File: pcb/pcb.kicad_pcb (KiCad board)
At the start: 2 copper layers, 173.5 x 140.5 mm, 75 parts, among them J1 RJ45, J2 RJ45, SW1 Keyswitch, SW10 Keyswitch, SW11 Keyswitch, SW12 Keyswitch, SW13 Keyswitch, SW14 Keyswitch, SW15 Keyswitch, SW16 Keyswitch, SW17 Keyswitch, SW18 Keyswitch, SW19 Keyswitch, SW2 Keyswitch, SW20 Keyswitch, SW21 Keyswitch, SW22 Keyswitch, SW23 Keyswitch, SW24 Keyswitch, SW25 Keyswitch, SW26 Keyswitch, SW27 Keyswitch, SW28 Keyswitch, SW29 Keyswitch, SW3 Keyswitch, SW30 Keyswitch, SW4 Keyswitch, SW5 Keyswitch, SW6 Keyswitch, SW7 Keyswitch, SW8 Keyswitch, SW9 Keyswitch

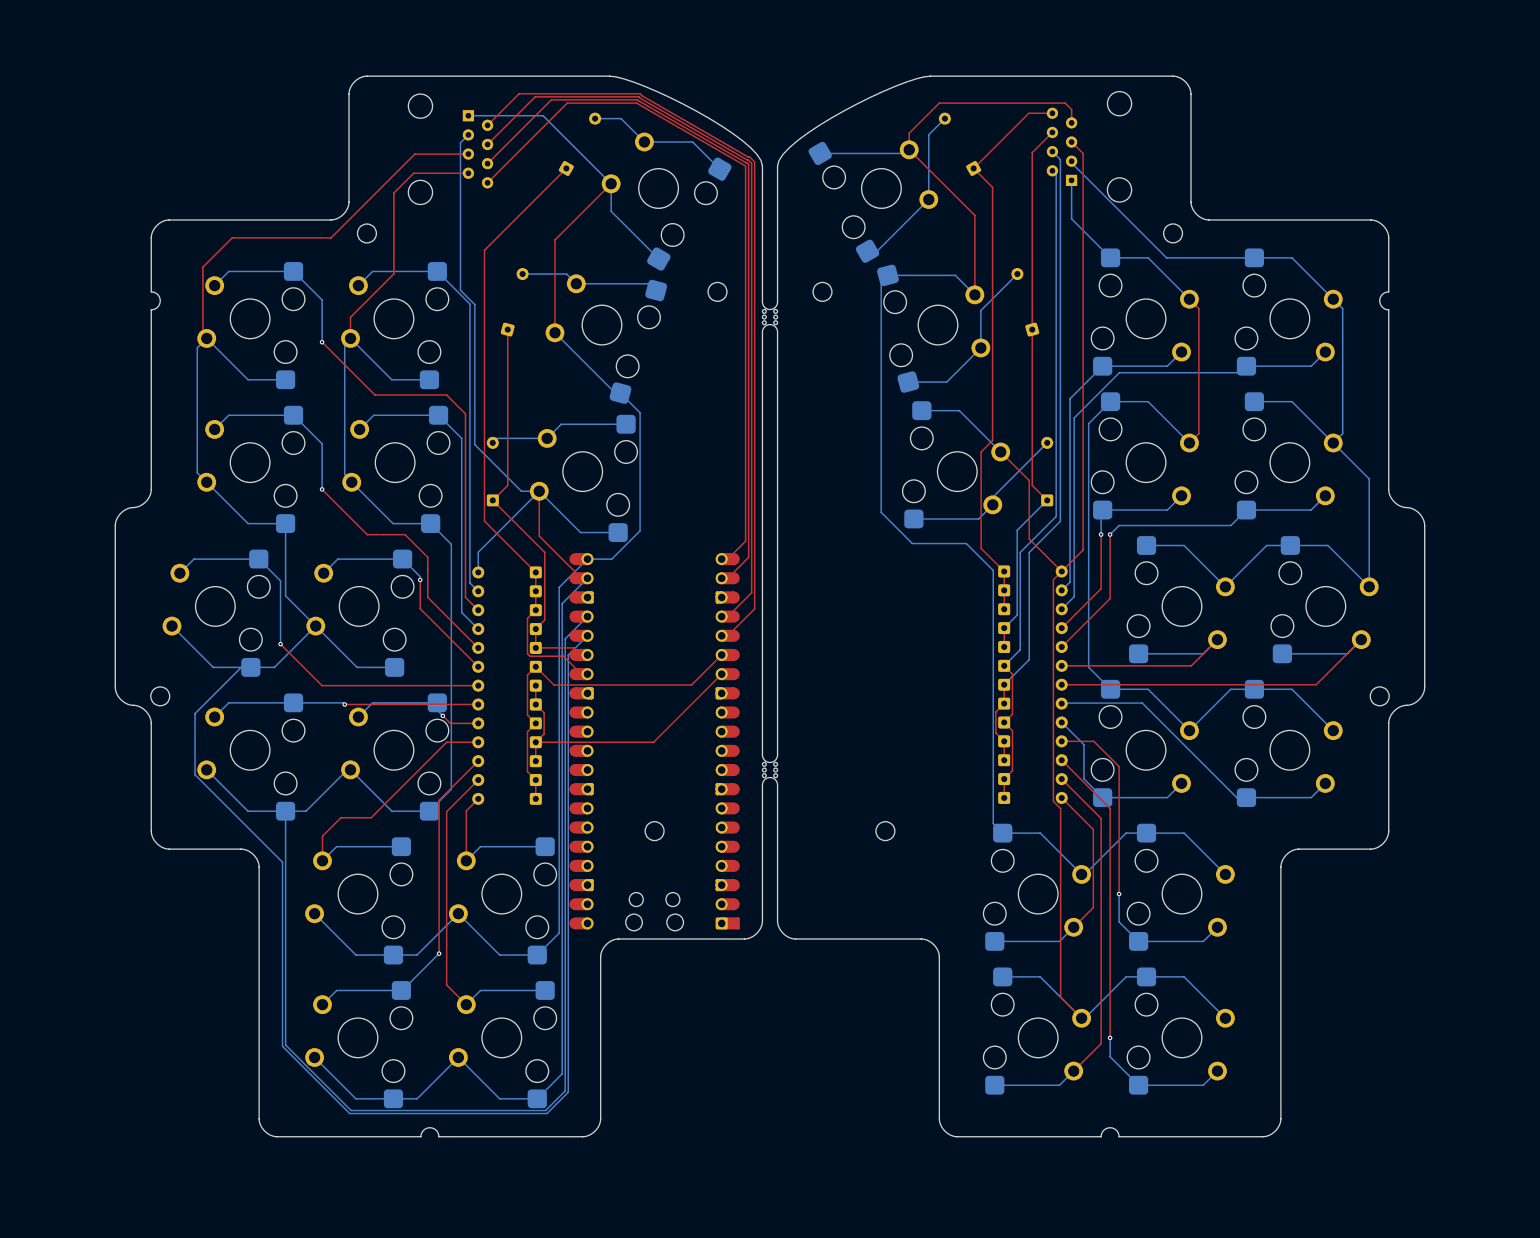
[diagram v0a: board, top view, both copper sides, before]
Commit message: add pcb filled zone
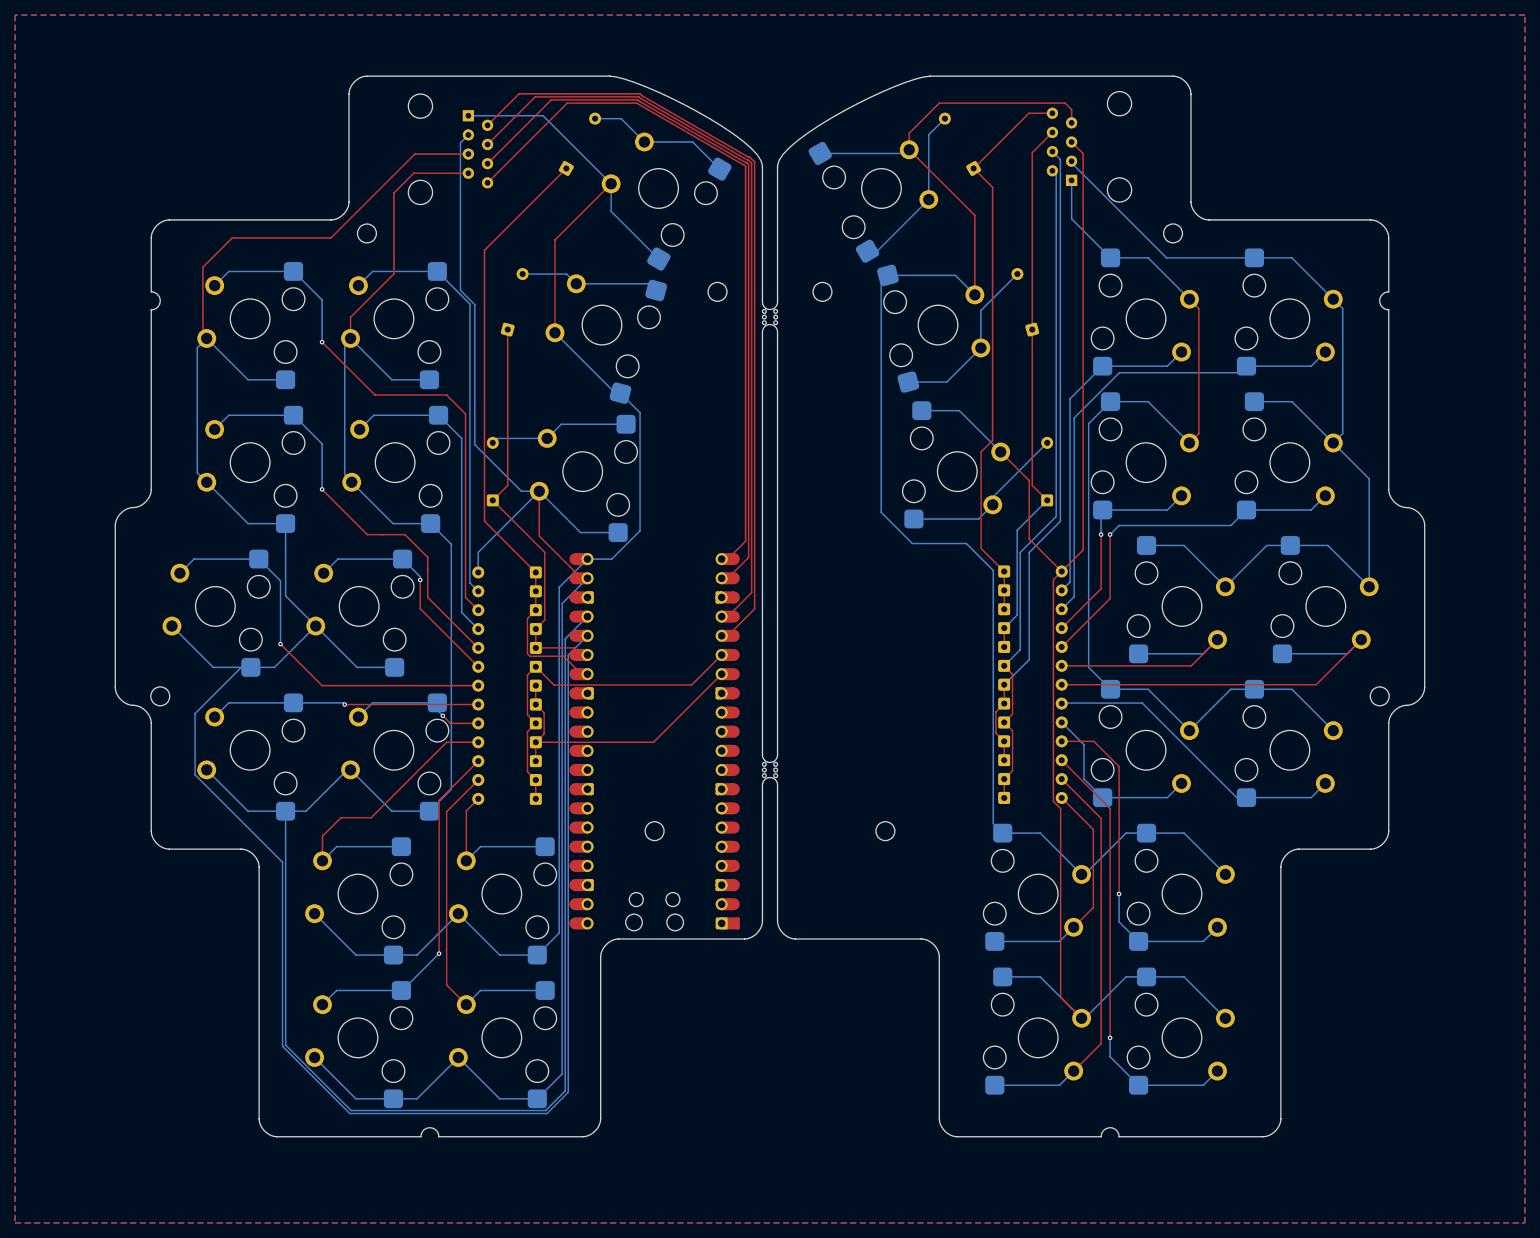
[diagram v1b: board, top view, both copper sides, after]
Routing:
- added copper zone on B.Cu, net (none)
- added copper zone on F.Cu, net (none)
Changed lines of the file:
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@@
 		(net 90)
+	)
+	(zone
+		(net 0)
+		(net_name "")
+		(layers "F.Cu" "B.Cu")
+		(hatch edge 0.5)
+		(connect_pads
+			(clearance 0.5)
+		)
+		(min_thickness 0.25)
+		(filled_areas_thickness no)
+		(fill yes
+			(mode hatch)
+			(thermal_gap 0.5)
+			(thermal_bridge_width 0.5)
+			(island_removal_mode 1)
+			(island_area_min 10)
+			(hatch_thickness 1)
+			(hatch_gap 1.5)
+			(hatch_orientation 45)
+			(hatch_border_algorithm hatch_thickness)
+			(hatch_min_hole_area 0.3)
+		)
+		(polygon
+			(pts
+				(xy 100 90) (xy 100 250) (xy 300 250) (xy 300 90)
+			)
+		)
 	)
 	(embedded_fonts no)
